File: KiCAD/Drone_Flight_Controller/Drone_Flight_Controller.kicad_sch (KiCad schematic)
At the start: 0 parts

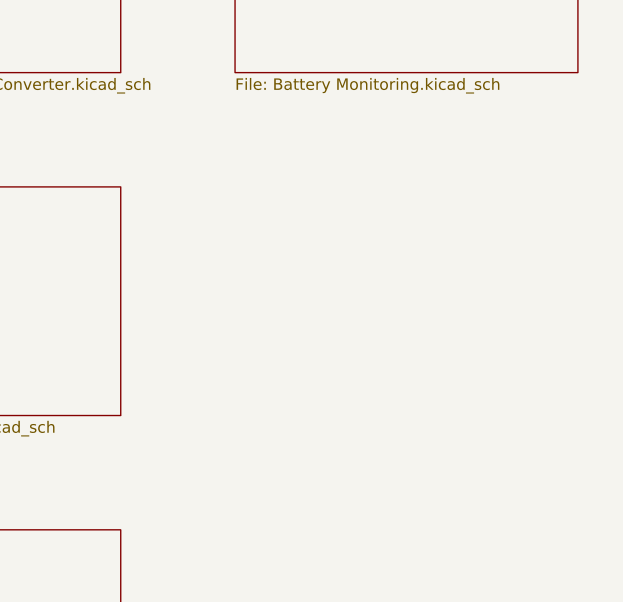
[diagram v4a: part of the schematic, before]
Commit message: Add USB & Status LEDs
Add USB & Status LEDs
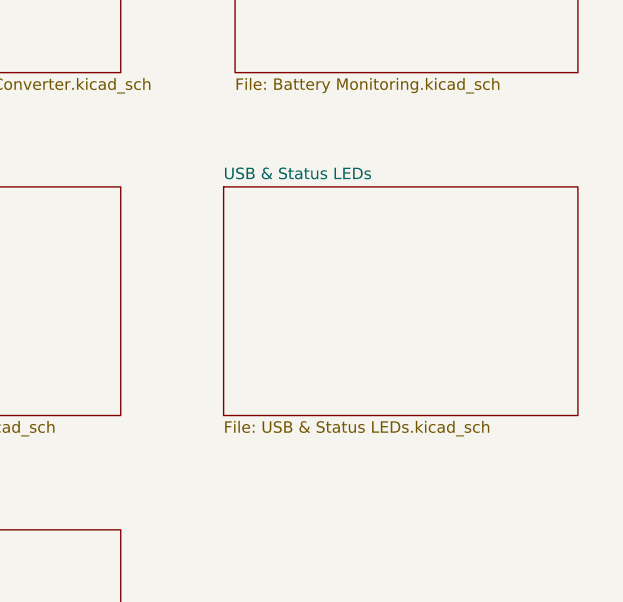
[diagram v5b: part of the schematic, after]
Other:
- added sheet USB & Status LEDs (USB & Status LEDs.kicad_sch)
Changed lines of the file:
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@@
+	)
+	(sheet
+		(at 74.93 63.5)
+		(size 39.37 25.4)
+		(exclude_from_sim no)
+		(in_bom yes)
+		(on_board yes)
+		(dnp no)
+		(fields_autoplaced yes)
+		(stroke
+			(width 0.1524)
+			(type solid)
+		)
+		(fill
+			(color 0 0 0 0.0000)
+		)
+		(property "Sheetname" "USB & Status LEDs"
+			(at 74.93 62.7884 0)
+			(effects
+				(font
+					(size 1.27 1.27)
+				)
+				(justify left bottom)
+			)
+		)
+		(property "Sheetfile" "USB & Status LEDs.kicad_sch"
+			(at 74.93 89.4846 0)
+			(effects
+				(font
+					(size 1.27 1.27)
+				)
+				(justify left top)
+			)
+		)
+		(instances
+			(project "Drone_Flight_Controller"
+				(path "/05daaa24-e506-4b9a-9564-8bf799413ca8"
+					(page "7")
+				)
+			)
+		)
 	)
 	(sheet

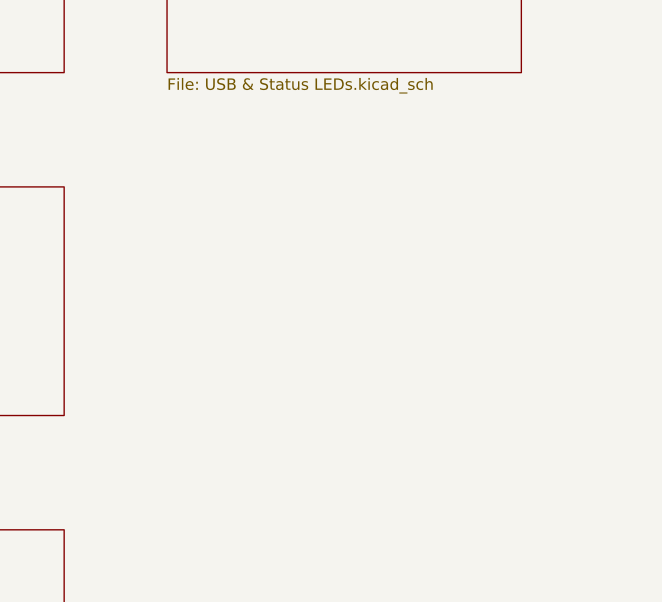
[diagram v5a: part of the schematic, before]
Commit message: Add 5V_to_3.3V_Voltage_Converter.kicad_sch
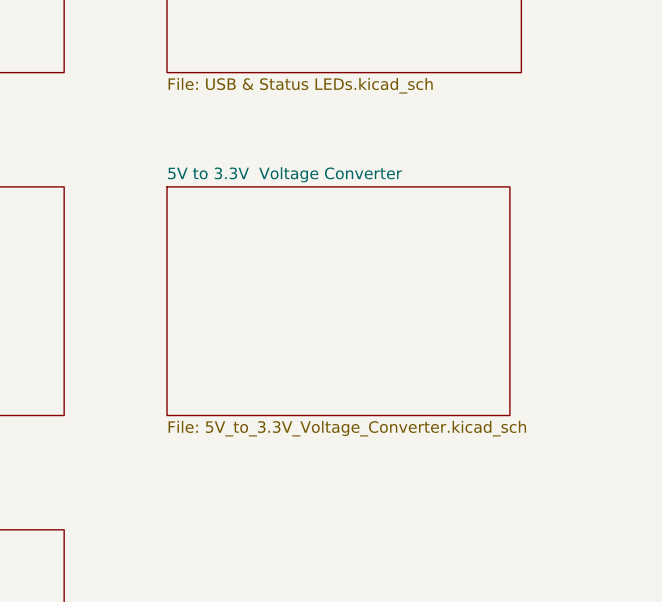
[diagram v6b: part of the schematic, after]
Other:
- added sheet 5V to 3.3V  Voltage Converter (5V_to_3.3V_Voltage_Converter.kicad_sch)
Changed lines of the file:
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@@
+	)
+	(sheet
+		(at 74.93 101.6)
+		(size 38.1 25.4)
+		(exclude_from_sim no)
+		(in_bom yes)
+		(on_board yes)
+		(dnp no)
+		(fields_autoplaced yes)
+		(stroke
+			(width 0.1524)
+			(type solid)
+		)
+		(fill
+			(color 0 0 0 0.0000)
+		)
+		(property "Sheetname" "5V to 3.3V  Voltage Converter"
+			(at 74.93 100.8884 0)
+			(effects
+				(font
+					(size 1.27 1.27)
+				)
+				(justify left bottom)
+			)
+		)
+		(property "Sheetfile" "5V_to_3.3V_Voltage_Converter.kicad_sch"
+			(at 74.93 127.5846 0)
+			(effects
+				(font
+					(size 1.27 1.27)
+				)
+				(justify left top)
+			)
+		)
+		(instances
+			(project "Drone_Flight_Controller"
+				(path "/05daaa24-e506-4b9a-9564-8bf799413ca8"
+					(page "8")
+				)
+			)
+		)
 	)
 	(sheet
